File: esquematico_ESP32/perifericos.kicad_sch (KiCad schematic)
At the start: 10 parts, among them J2 Conn_RFID1, J3 Conn_RFID2, J4 USB_A, J5 Conn_screen, J6 Conn_01x04_Female

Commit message: ruteo listo con un posible error en footprint esp32
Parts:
- J2, J3: footprint (none) -> Connector_JST:JST_EH_S8B-EH_1x08_P2.50mm_Horizontal
- J5: footprint (none) -> Connector_JST:JST_EH_S10B-EH_1x10_P2.50mm_Horizontal
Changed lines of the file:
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@@
       (effects (font (size 1.27 1.27)) (justify right))
     )
-    (property "Footprint" "" (id 2) (at 78.74 67.31 0)
+    (property "Footprint" "Connector_JST:JST_EH_S8B-EH_1x08_P2.50mm_Horizontal" (id 2) (at 78.74 67.31 0)
       (effects (font (size 1.27 1.27)) hide)
     )
@@
       (effects (font (size 1.27 1.27)) (justify right))
     )
-    (property "Footprint" "" (id 2) (at 78.74 39.37 0)
+    (property "Footprint" "Connector_JST:JST_EH_S8B-EH_1x08_P2.50mm_Horizontal" (id 2) (at 78.74 39.37 0)
       (effects (font (size 1.27 1.27)) hide)
     )
@@
       (effects (font (size 1.27 1.27)) (justify right))
     )
-    (property "Footprint" "" (id 2) (at 119.38 57.15 0)
+    (property "Footprint" "Connector_JST:JST_EH_S10B-EH_1x10_P2.50mm_Horizontal" (id 2) (at 119.38 57.15 0)
       (effects (font (size 1.27 1.27)) hide)
     )

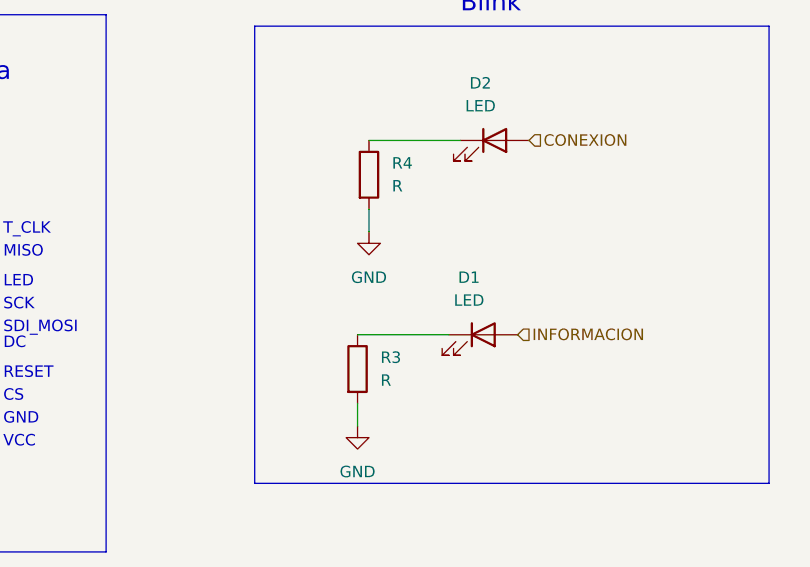
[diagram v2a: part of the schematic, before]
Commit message: se agregaron los valores (pendiente última revisión)
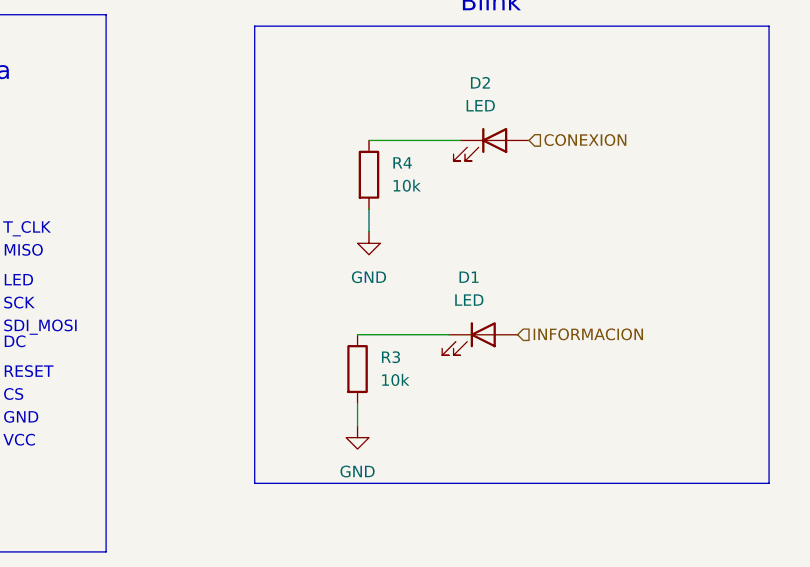
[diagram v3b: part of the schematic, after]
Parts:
- R3, R4: value R -> 10k
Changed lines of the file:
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@@
       (effects (font (size 1.27 1.27)) (justify left))
     )
-    (property "Value" "R" (id 1) (at 163.83 39.3699 0)
+    (property "Value" "10k" (id 1) (at 163.83 39.3699 0)
       (effects (font (size 1.27 1.27)) (justify left))
     )
@@
       (effects (font (size 1.27 1.27)) (justify left))
     )
-    (property "Value" "R" (id 1) (at 162.56 60.9599 0)
+    (property "Value" "10k" (id 1) (at 162.56 60.9599 0)
       (effects (font (size 1.27 1.27)) (justify left))
     )

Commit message: Alternativa_Acomodada
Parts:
- Conn_RFID1: renamed from J2; value Conn_RFID1 -> J2
- Conn_RFID2: renamed from J3; value Conn_RFID2 -> J3
- Conn_screen1: renamed from J5; value Conn_screen -> J5
- D1, D2: footprint LED_SMD:LED_1206_3216Metric_Pad1.42x1.75mm_HandSolder -> LED_SMD:LED_0805_2012Metric_Pad1.15x1.40mm_HandSolder
- renumbered J6 to Sensitizer1, J4 to Teclado1
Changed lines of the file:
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@@
     (property "Reference" "D2" (id 0) (at 173.6725 27.94 0))
     (property "Value" "LED" (id 1) (at 173.6725 30.48 0))
-    (property "Footprint" "LED_SMD:LED_1206_3216Metric_Pad1.42x1.75mm_HandSolder" (id 2) (at 175.26 34.29 0)
+    (property "Footprint" "LED_SMD:LED_0805_2012Metric_Pad1.15x1.40mm_HandSolder" (id 2) (at 175.26 34.29 0)
       (effects (font (size 1.27 1.27)) hide)
     )
@@
   (symbol (lib_id "Connector:Conn_01x04_Female") (at 247.65 45.72 0) (unit 1)
     (in_bom yes) (on_board yes)
-    (property "Reference" "J6" (id 0) (at 243.84 53.34 0)
+    (property "Reference" "Sensitizer1" (id 0) (at 243.84 53.34 0)
       (effects (font (size 1.27 1.27)) (justify left))
     )
@@
   (symbol (lib_id "Connector:Conn_01x08_Male") (at 78.74 67.31 0) (mirror y) (unit 1)
     (in_bom yes) (on_board yes) (fields_autoplaced)
-    (property "Reference" "J3" (id 0) (at 80.01 67.3099 0)
-      (effects (font (size 1.27 1.27)) (justify right))
-    )
-    (property "Value" "Conn_RFID2" (id 1) (at 80.01 69.8499 0)
+    (property "Reference" "Conn_RFID2" (id 0) (at 80.01 67.3099 0)
+      (effects (font (size 1.27 1.27)) (justify right))
+    )
+    (property "Value" "J3" (id 1) (at 80.01 69.8499 0)
       (effects (font (size 1.27 1.27)) (justify right))
     )
@@
     (property "Reference" "D1" (id 0) (at 172.4025 49.53 0))
     (property "Value" "LED" (id 1) (at 172.4025 52.07 0))
-    (property "Footprint" "LED_SMD:LED_1206_3216Metric_Pad1.42x1.75mm_HandSolder" (id 2) (at 173.99 55.88 0)
+    (property "Footprint" "LED_SMD:LED_0805_2012Metric_Pad1.15x1.40mm_HandSolder" (id 2) (at 173.99 55.88 0)
       (effects (font (size 1.27 1.27)) hide)
     )
@@
   (symbol (lib_id "Connector:USB_A") (at 101.6 133.35 0) (unit 1)
     (in_bom yes) (on_board yes) (fields_autoplaced)
-    (property "Reference" "J4" (id 0) (at 101.6 120.65 0))
+    (property "Reference" "Teclado1" (id 0) (at 101.6 120.65 0))
     (property "Value" "USB_A" (id 1) (at 101.6 123.19 0))
     (property "Footprint" "Connector_USB:USB_A_Molex_67643_Horizontal" (id 2) (at 105.41 134.62 0)
@@
   (symbol (lib_id "Connector:Conn_01x08_Male") (at 78.74 39.37 0) (mirror y) (unit 1)
     (in_bom yes) (on_board yes) (fields_autoplaced)
-    (property "Reference" "J2" (id 0) (at 80.01 39.3699 0)
-      (effects (font (size 1.27 1.27)) (justify right))
-    )
-    (property "Value" "Conn_RFID1" (id 1) (at 80.01 41.9099 0)
+    (property "Reference" "Conn_RFID1" (id 0) (at 80.01 39.3699 0)
+      (effects (font (size 1.27 1.27)) (justify right))
+    )
+    (property "Value" "J2" (id 1) (at 80.01 41.9099 0)
       (effects (font (size 1.27 1.27)) (justify right))
     )
@@
   (symbol (lib_id "Connector:Conn_01x10_Male") (at 119.38 57.15 180) (unit 1)
     (in_bom yes) (on_board yes)
-    (property "Reference" "J5" (id 0) (at 107.95 74.93 0)
-      (effects (font (size 1.27 1.27)) (justify right))
-    )
-    (property "Value" "Conn_screen" (id 1) (at 106.68 72.39 0)
-      (effects (font (size 1.27 1.27)) (justify right))
-    )
+    (property "Reference" "Conn_screen1" (id 0) (at 107.95 74.93 0)
+      (effects (font (size 1.27 1.27)) (justify right))
+    )
+    (property "Value" "J5" (id 1) (at 106.68 72.39 0)
+      (effects (font (size 1.27 1.27)) (justify right))
+    )

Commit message: placa terminada
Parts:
- renumbered Conn_RFID1 to RFID1, Conn_RFID2 to RFID2, Conn_screen1 to screen1
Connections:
- net MAGNE_4 is gone; now on net MAGNE_2: Sensitizer1.1 (Pin_1)
- net MAGNE_2: no longer Sensitizer1.3 (Pin_3)
- net MAGNE_3: now also Sensitizer1.3 (Pin_3); no longer Sensitizer1.2 (Pin_2)
- new net MAGNE_1: Sensitizer1.2 (Pin_2)
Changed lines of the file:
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@@
     (effects (font (size 1.27 1.27)) (justify right))
   )
-  (hierarchical_label "MAGNE_4" (shape input) (at 242.57 43.18 180)
+  (hierarchical_label "MAGNE_1" (shape input) (at 242.57 45.72 180)
     (effects (font (size 1.27 1.27)) (justify right))
   )
@@
     (effects (font (size 1.27 1.27)) (justify right))
   )
-  (hierarchical_label "MAGNE_3" (shape input) (at 242.57 45.72 180)
+  (hierarchical_label "MAGNE_3" (shape input) (at 242.57 48.26 180)
     (effects (font (size 1.27 1.27)) (justify right))
   )
@@
     (effects (font (size 1.27 1.27)) (justify right))
   )
-  (hierarchical_label "MAGNE_2" (shape input) (at 242.57 48.26 180)
+  (hierarchical_label "MAGNE_2" (shape input) (at 242.57 43.18 180)
     (effects (font (size 1.27 1.27)) (justify right))
   )
@@
   (symbol (lib_id "Connector:Conn_01x08_Male") (at 78.74 67.31 0) (mirror y) (unit 1)
     (in_bom yes) (on_board yes) (fields_autoplaced)
-    (property "Reference" "Conn_RFID2" (id 0) (at 80.01 67.3099 0)
+    (property "Reference" "RFID2" (id 0) (at 80.01 67.3099 0)
       (effects (font (size 1.27 1.27)) (justify right))
     )
@@
   (symbol (lib_id "Connector:Conn_01x08_Male") (at 78.74 39.37 0) (mirror y) (unit 1)
     (in_bom yes) (on_board yes) (fields_autoplaced)
-    (property "Reference" "Conn_RFID1" (id 0) (at 80.01 39.3699 0)
+    (property "Reference" "RFID1" (id 0) (at 80.01 39.3699 0)
       (effects (font (size 1.27 1.27)) (justify right))
     )
@@
   (symbol (lib_id "Connector:Conn_01x10_Male") (at 119.38 57.15 180) (unit 1)
     (in_bom yes) (on_board yes)
-    (property "Reference" "Conn_screen1" (id 0) (at 107.95 74.93 0)
-      (effects (font (size 1.27 1.27)) (justify right))
-    )
+    (property "Reference" "screen1" (id 0) (at 107.95 74.93 0)
+      (effects (font (size 1.27 1.27)) (justify right))
+    )
